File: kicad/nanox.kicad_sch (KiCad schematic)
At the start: 137 parts, among them P1 likely an ESD protection diod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, P2 likely an ESD protection diod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, P3 likely an ESD protection diod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, P4 likely an ESD protection diod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, P5 likely an ESD protection diod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, SW1 push button, left, SW2 push button, right, X1 ?, X10 unknown, marked 1C4F, likely 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, X2 unknown, marked 2GC, X3 unknown, marked 6, X4 ?, X5 ?, X6 ?, X7 ?, X8 ?, X9 unknown, marked P8W 26, Y1 crystal, likely the 32 MHz HSE

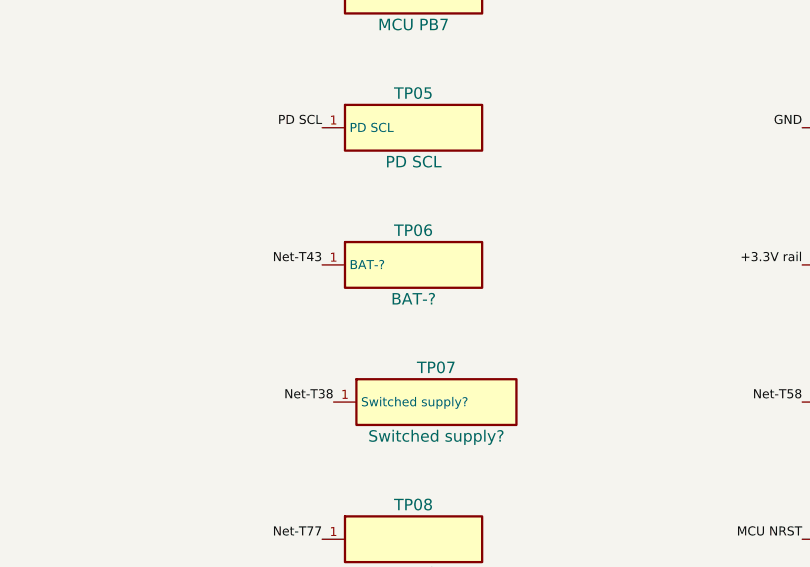
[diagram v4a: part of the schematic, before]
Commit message: Route specimen B's leg past PWR3 onto battery pads 2 and 3, add its SPI taps
The leg runs straight from the board's edge to PWR3, then turns 90 degrees
onto battery pad 2, with a short branch onto pad 3 just past the fold.
Battery pad 1 (Net-T43) is likely the temperature sensor, so TP06 is
renamed BAT NTC? and the battery pad notes say which is which. The flex
gets round, hand-soldered holes over the OLED SPI CS, CLK and MOSI test
pads (TP31, TP34, TP35).

Co-Authored-By: Claude Opus 5.5 <noreply@anthropic.com>
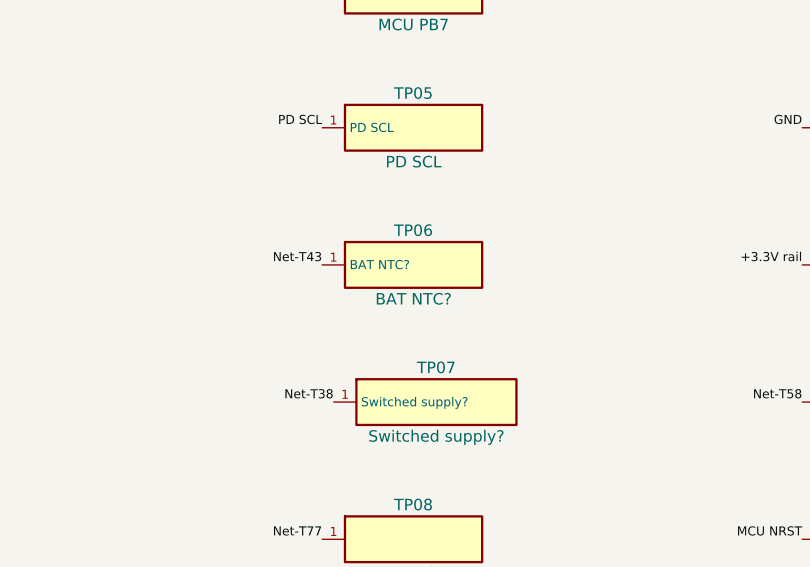
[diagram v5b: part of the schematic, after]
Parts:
- TP06: value BAT-? -> BAT NTC?
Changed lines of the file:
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@@
  (symbol (lib_id "nanox:TP06") (at 337.82 180.34 0) (unit 1) (in_bom yes) (on_board yes) (dnp no)
   (property "Reference" "TP06" (at 337.82 176.53 0) (effects (font (size 1.27 1.27))))
-  (property "Value" "BAT-?" (at 337.82 184.15 0) (effects (font (size 1.27 1.27))))
+  (property "Value" "BAT NTC?" (at 337.82 184.15 0) (effects (font (size 1.27 1.27))))
   (property "Footprint" "" (at 337.82 180.34 0) (effects (font (size 1.27 1.27)) hide))
   (property "Description" "test pad" (at 337.82 180.34 0) (effects (font (size 1.27 1.27)) hide))

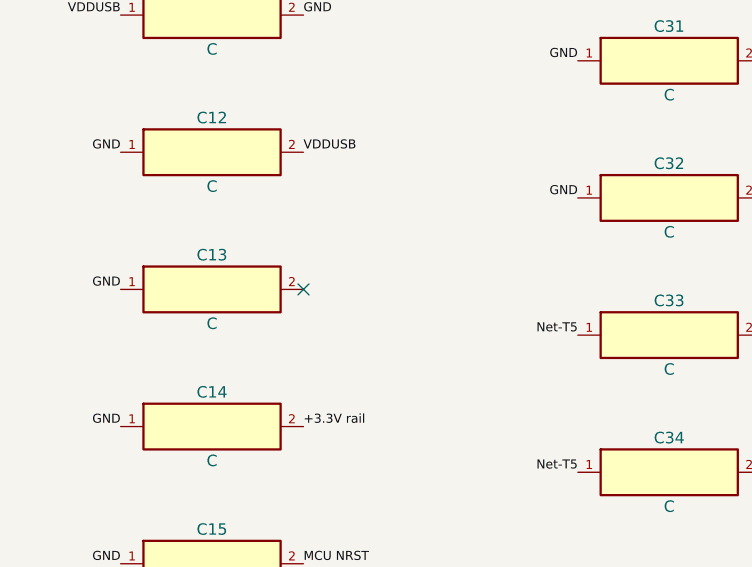
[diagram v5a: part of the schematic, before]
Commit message: Connect C13 to +3.3V and give the LSE traces more room
The +3.3V branch to MCU pin 1 now starts on C13's free pad and runs at
45 degrees from there, so C13 decouples the rail as on the real board.
That frees room to move LSE crystal IN and OUT further left: LSE OUT is
now 0.63 mm from the +3.3V via's centre.

Co-Authored-By: Claude Opus 5.5 <noreply@anthropic.com>
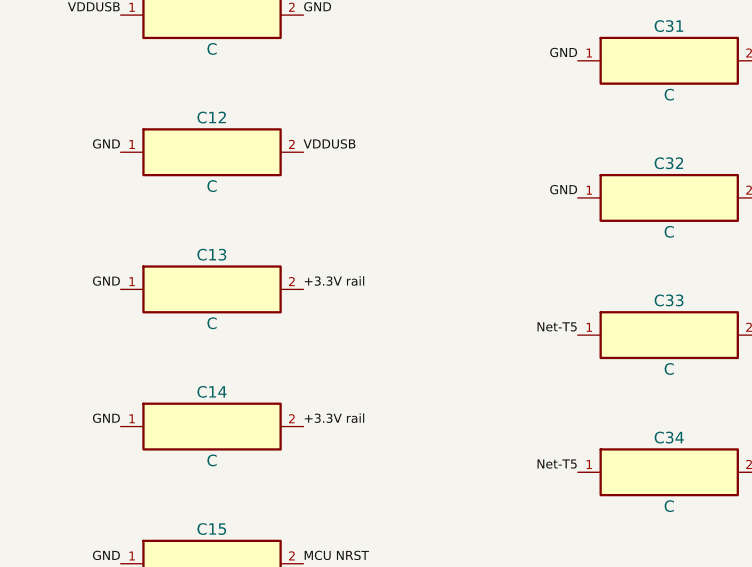
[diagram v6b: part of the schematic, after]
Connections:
- net +3.3V rail: now also C13.2
- no-connect marks 64 -> 63
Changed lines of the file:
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@@
  )
  (label "GND" (at 25.40 160.02 180) (effects (font (size 1.0 1.0)) (justify right bottom)))
- (no_connect (at 45.72 160.02))
+ (label "+3.3V rail" (at 45.72 160.02 0) (effects (font (size 1.0 1.0)) (justify left bottom)))
  (symbol (lib_id "nanox:C14") (at 35.56 175.26 0) (unit 1) (in_bom yes) (on_board yes) (dnp no)
   (property "Reference" "C14" (at 35.56 171.45 0) (effects (font (size 1.27 1.27))))

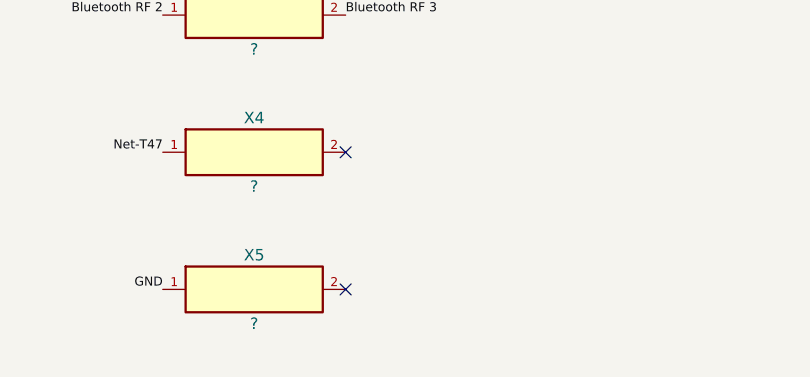
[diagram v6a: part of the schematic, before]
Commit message: Clear the remaining copper overlaps in the KiCad board
- X5 pad 2 joins Bluetooth RF 3: the trace corner sat 3 px outside it, so
  the shunt part on the antenna side of the matching network floated
- Net-T46 leaves R6 pad 1 at 45 degrees, clear of pad 2
- I2C1 SDA runs 3 px further left past C15, where the copper is
- +3.3V moves 4 px left past RFF1, and 6 px down under Net-T5's via
- Left button dips under the OLED MOSI via instead of grazing it

KiCad now reports no shorts.

Co-Authored-By: Claude Opus 5.5 <noreply@anthropic.com>
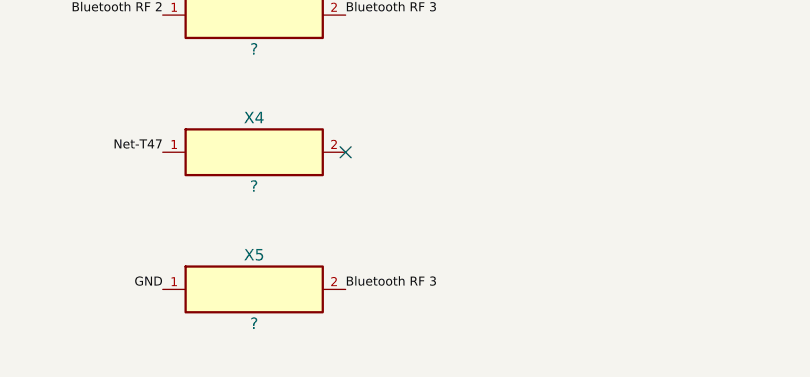
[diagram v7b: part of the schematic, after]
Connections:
- net Bluetooth RF 3: now also X5.2
- no-connect marks 63 -> 62
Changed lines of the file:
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@@
  )
  (label "GND" (at 439.42 294.64 180) (effects (font (size 1.0 1.0)) (justify right bottom)))
- (no_connect (at 459.74 294.64))
+ (label "Bluetooth RF 3" (at 459.74 294.64 0) (effects (font (size 1.0 1.0)) (justify left bottom)))
  (symbol (lib_id "nanox:X6") (at 513.08 27.94 0) (unit 1) (in_bom yes) (on_board yes) (dnp no)
   (property "Reference" "X6" (at 513.08 24.13 0) (effects (font (size 1.27 1.27))))

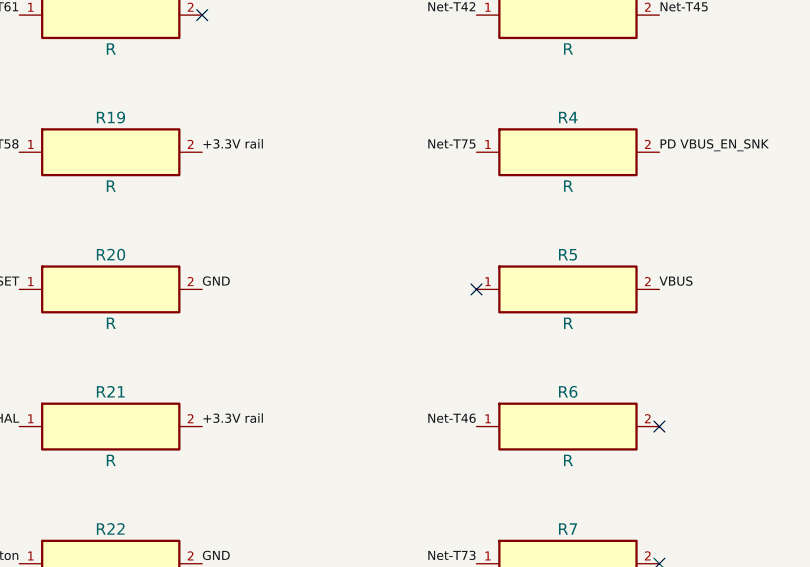
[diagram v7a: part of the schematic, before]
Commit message: Align the MCU's traces with its pins
Every trace on an MCU pin now ends on the pin's centre with a final run
perpendicular to the package edge, turning at 45 degrees onto its old
route. Detours and stubs around pins 12, 13, 18, 37 and 48 are gone, and
the traces that stopped short of pins 8, 13, 17 and 20 now reach them.

Also lands PD VBUS_VS_DISCH on R5, the discharge resistor to VBUS: the
trace ran across R5's pad without connecting, which KiCad saw as a short.

Co-Authored-By: Claude Opus 5.5 <noreply@anthropic.com>
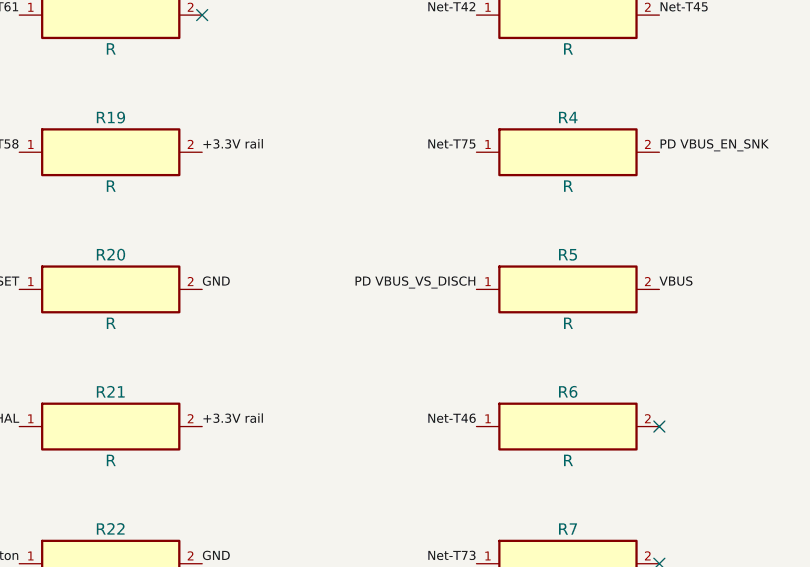
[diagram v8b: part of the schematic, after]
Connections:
- net PD VBUS_VS_DISCH: now also R5.1
- no-connect marks 62 -> 61
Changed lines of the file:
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@@
   (instances (project "nanox" (path "/9fc871f3-1e36-5a01-9359-e2a20c86f96f" (reference "R5") (unit 1))))
  )
- (no_connect (at 236.22 180.34))
+ (label "PD VBUS_VS_DISCH" (at 236.22 180.34 180) (effects (font (size 1.0 1.0)) (justify right bottom)))
  (label "VBUS" (at 256.54 180.34 0) (effects (font (size 1.0 1.0)) (justify left bottom)))
  (symbol (lib_id "nanox:R6") (at 246.38 195.58 0) (unit 1) (in_bom yes) (on_board yes) (dnp no)
